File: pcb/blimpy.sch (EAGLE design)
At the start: 74 parts, among them J4 3-PIN SMD, J5 3-PIN SMD, J6 3-PIN SMD, J7 3-PIN SMD, Q1 mmbt2222, Q2 mmbt2222, Q3 DMG3415U, U1 RGB, U10 MAX17048, U2 AP2112-3.3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

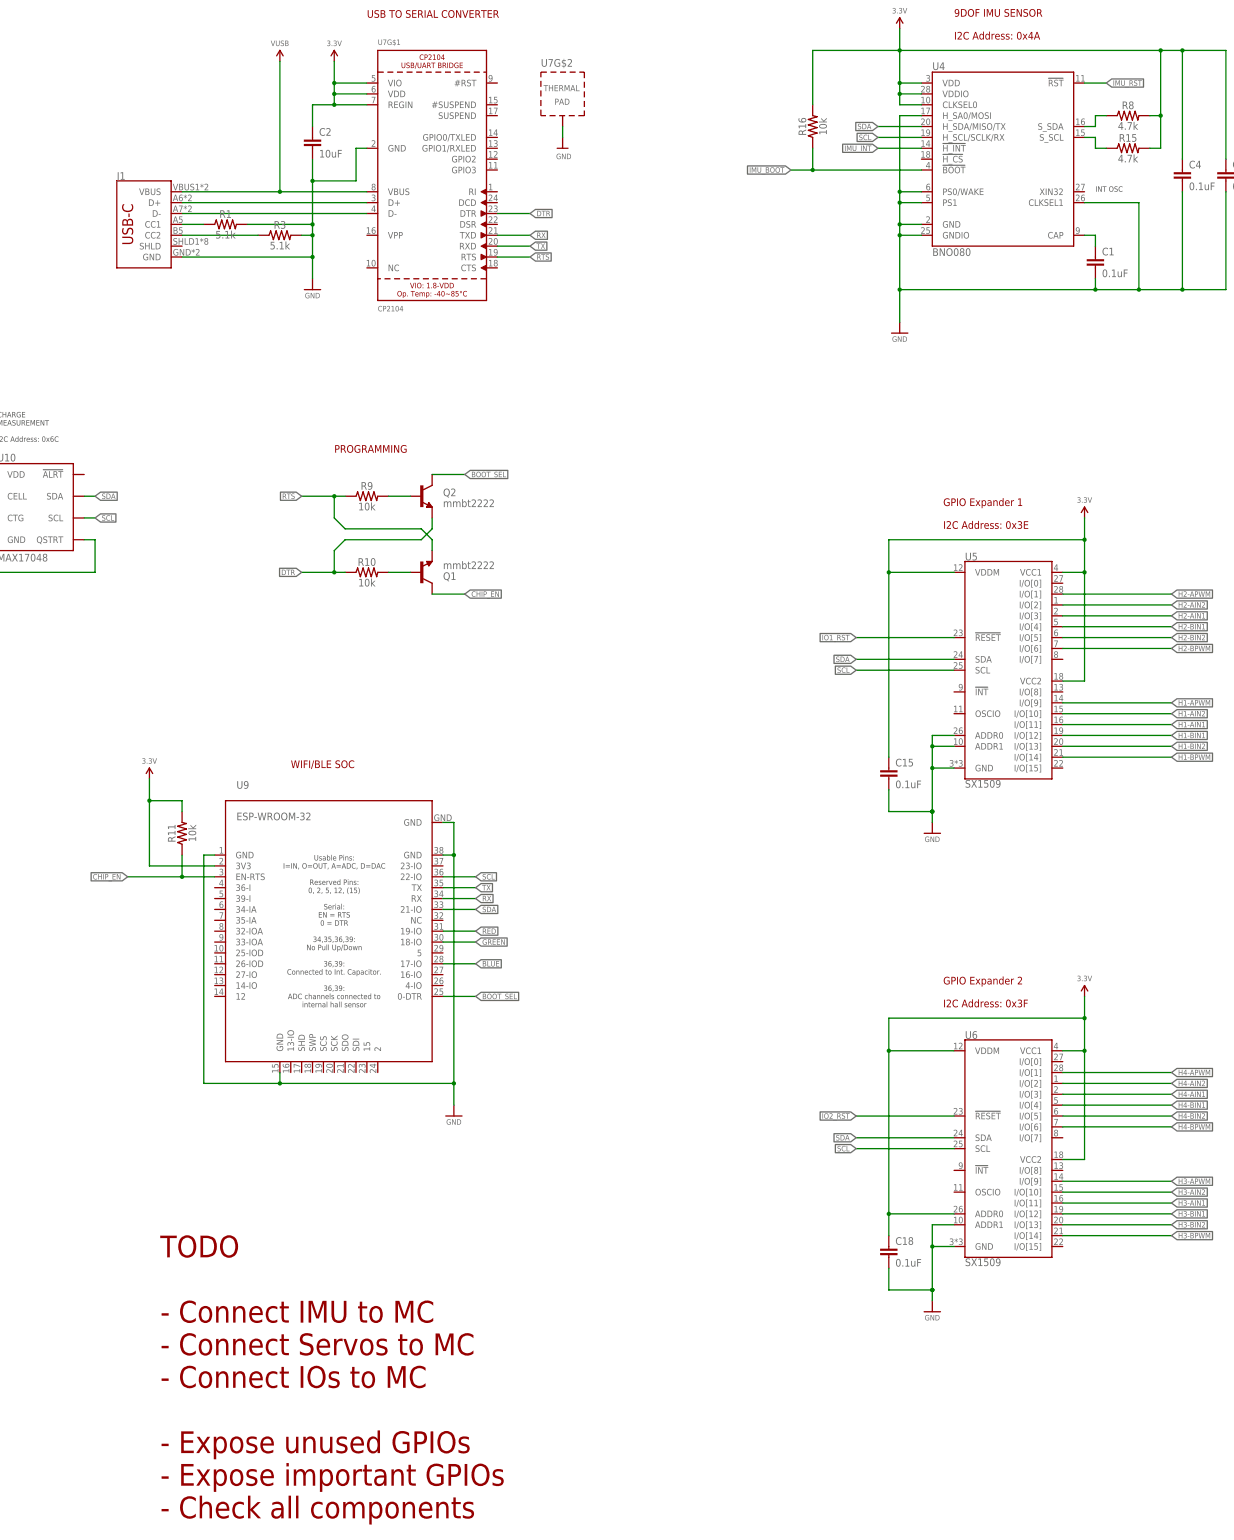
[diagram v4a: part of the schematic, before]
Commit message: connected all components
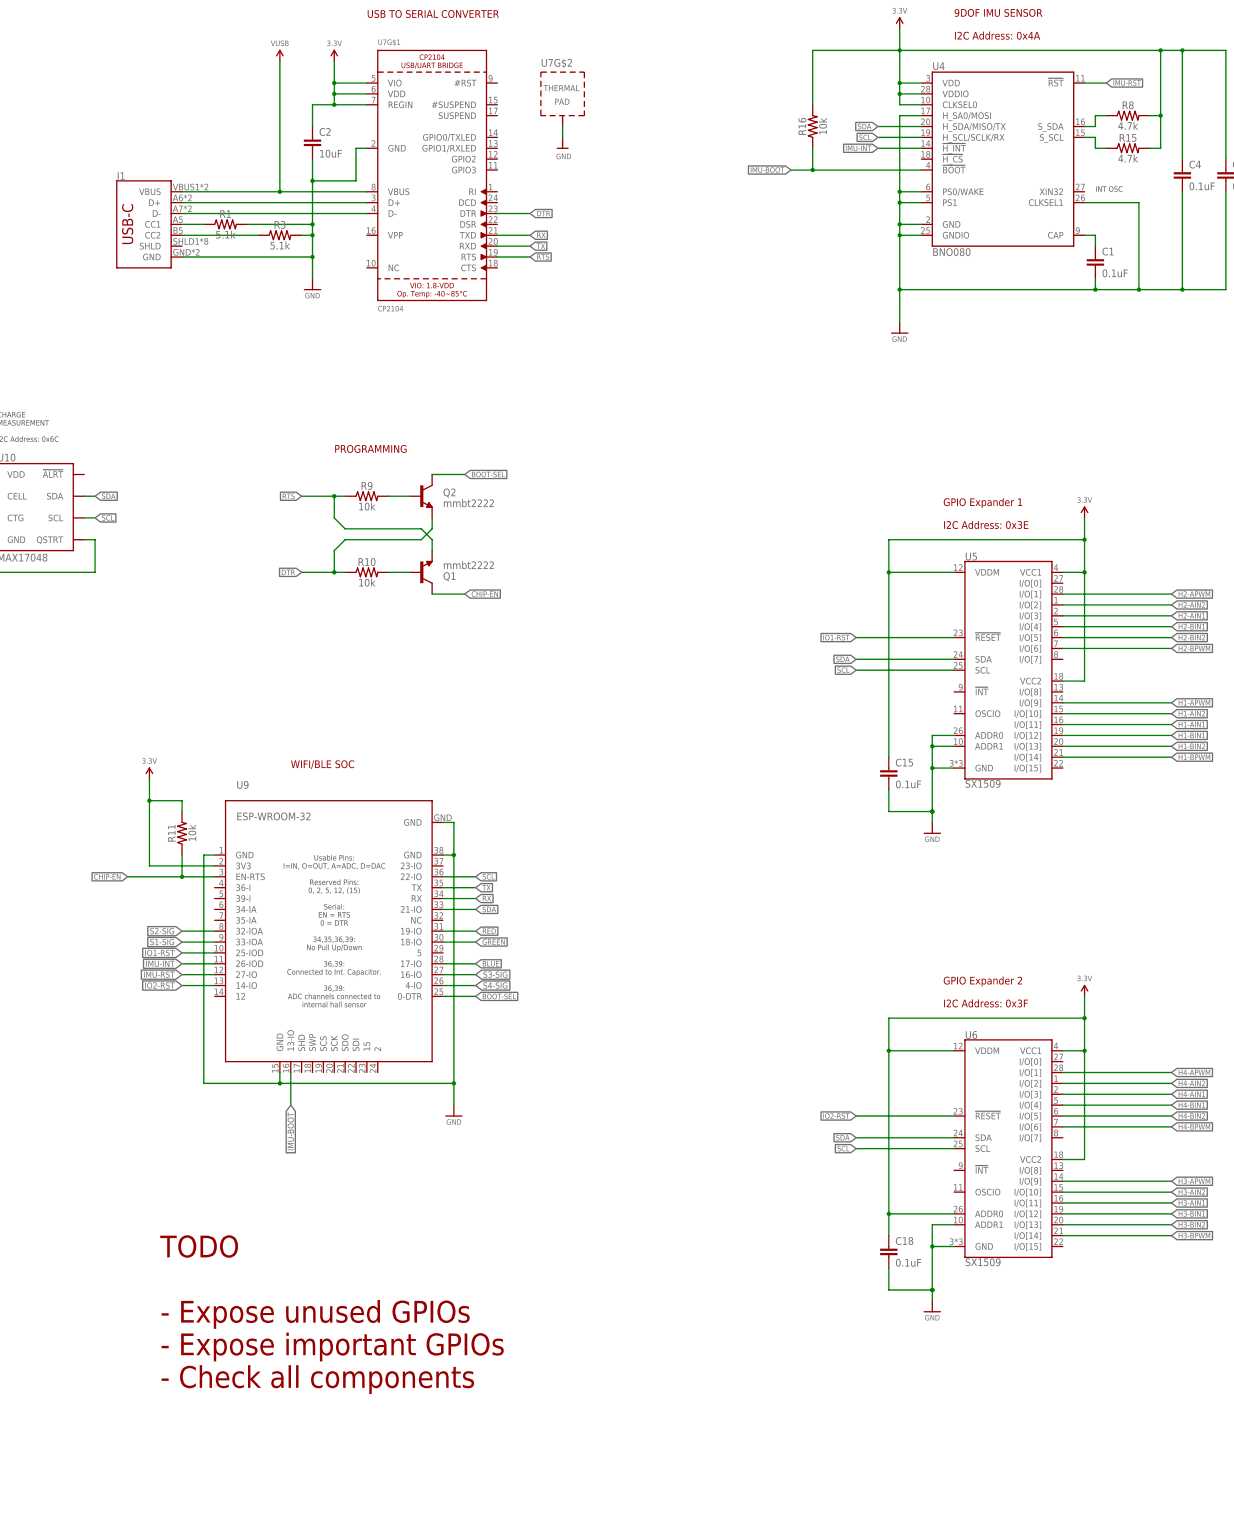
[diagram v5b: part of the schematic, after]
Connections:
- net BOOT_SEL renamed BOOT-SEL
- net CHIP_EN renamed CHIP-EN
- removed net IMU_BOOT: R16.1, U4.!BOOT
- removed net IMU_INT: U4.!H_INT
- removed net IMU_RST: U4.!RST
- removed net IO1_RST: U5.!RESET
- removed net IO2_RST: U6.!RESET
- new net IMU-BOOT: R16.1, U4.!BOOT, U9.13-IO
- new net IMU-INT: U4.!H_INT, U9.26-IOD
- new net IMU-RST: U4.!RST, U9.27-IO
- new net IO1-RST: U5.!RESET, U9.25-IOD
- new net IO2-RST: U6.!RESET, U9.14-IO
- net S1-SIG: now also U9.33-IOA
- net S2-SIG: now also U9.32-IOA
- net S3-SIG: now also U9.16-IO
- net S4-SIG: now also U9.4-IO
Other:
- note added: "TODO - Expose unused GPIOs - Expose important GPIOs - Check all components"
- note removed: "TODO - Connect IMU to MC - Connect Servos to MC - Connect IOs to MC - Expose unused GPIOs - Expose important GPIOs - Check all components"
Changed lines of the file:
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@@
 <text x="378.46" y="185.42" size="1.27" layer="97">INT OSC</text>
 <text x="160.02" y="-58.42" size="5.08" layer="94" align="top-left">TODO
-- Connect IMU to MC
-- Connect Servos to MC
-- Connect IOs to MC
 - Expose unused GPIOs
 - Expose important GPIOs
@@
 </segment>
 </net>
-<net name="BOOT_SEL" class="0">
-<segment>
-<wire x1="223.52" y1="119.38" x2="231.14" y2="119.38" width="0.1524" layer="91"/>
-<pinref part="Q2" gate="G$1" pin="C"/>
-<label x="231.14" y="119.38" size="1.27" layer="95" xref="yes"/>
-</segment>
-<segment>
-<pinref part="U9" gate="G$1" pin="0-DTR"/>
-<wire x1="226.06" y1="-2.54" x2="233.68" y2="-2.54" width="0.1524" layer="91"/>
-<label x="233.68" y="-2.54" size="1.27" layer="95" xref="yes"/>
-</segment>
-</net>
 <net name="N$2" class="0">
 <segment>
@@
 </segment>
 </net>
-<net name="CHIP_EN" class="0">
-<segment>
-<pinref part="U9" gate="G$1" pin="EN-RTS"/>
-<wire x1="172.72" y1="25.4" x2="165.1" y2="25.4" width="0.1524" layer="91"/>
-<label x="152.4" y="25.4" size="1.27" layer="95" rot="MR0" xref="yes"/>
-<wire x1="165.1" y1="25.4" x2="152.4" y2="25.4" width="0.1524" layer="91"/>
-<wire x1="165.1" y1="30.48" x2="165.1" y2="25.4" width="0.1524" layer="91"/>
-<junction x="165.1" y="25.4"/>
-<pinref part="R11" gate="G$1" pin="1"/>
-</segment>
-<segment>
-<wire x1="231.14" y1="91.44" x2="223.52" y2="91.44" width="0.1524" layer="91"/>
-<pinref part="Q1" gate="G$1" pin="C"/>
-<label x="231.14" y="91.44" size="1.27" layer="95" xref="yes"/>
-</segment>
-</net>
 <net name="RED" class="0">
 <segment>
@@
 </segment>
 </net>
-<net name="IMU_INT" class="0">
-<segment>
-<pinref part="U4" gate="U1" pin="!H_INT"/>
-<wire x1="337.82" y1="195.58" x2="327.66" y2="195.58" width="0.1524" layer="91"/>
-<label x="327.66" y="195.58" size="1.27" layer="95" rot="R180" xref="yes"/>
-</segment>
-</net>
-<net name="IMU_BOOT" class="0">
+<net name="IMU-BOOT" class="0">
 <segment>
 <pinref part="U4" gate="U1" pin="!BOOT"/>
@@
 <junction x="312.42" y="190.5"/>
 </segment>
-</net>
-<net name="IMU_RST" class="0">
-<segment>
-<pinref part="U4" gate="U1" pin="!RST"/>
-<wire x1="375.92" y1="210.82" x2="381" y2="210.82" width="0.1524" layer="91"/>
-<label x="381" y="210.82" size="1.27" layer="95" xref="yes"/>
+<segment>
+<pinref part="U9" gate="G$1" pin="13-IO"/>
+<wire x1="190.5" y1="-20.32" x2="190.5" y2="-27.94" width="0.1524" layer="91"/>
+<label x="190.5" y="-27.94" size="1.4224" layer="95" rot="R270" xref="yes"/>
 </segment>
 </net>
@@
 </segment>
 </net>
-<net name="IO2_RST" class="0">
+<net name="IO2-RST" class="0">
 <segment>
 <wire x1="322.58" y1="-30.48" x2="345.44" y2="-30.48" width="0.1524" layer="91"/>
@@
 <label x="322.58" y="-30.48" size="1.27" layer="95" rot="R180" xref="yes"/>
 </segment>
-</net>
-<net name="IO1_RST" class="0">
-<segment>
-<wire x1="322.58" y1="81.28" x2="345.44" y2="81.28" width="0.1524" layer="91"/>
-<pinref part="U5" gate="G$1" pin="!RESET"/>
-<label x="322.58" y="81.28" size="1.27" layer="95" rot="R180" xref="yes"/>
+<segment>
+<pinref part="U9" gate="G$1" pin="14-IO"/>
+<wire x1="172.72" y1="0" x2="165.1" y2="0" width="0.1524" layer="91"/>
+<label x="165.1" y="0" size="1.4224" layer="95" rot="R180" xref="yes"/>
 </segment>
 </net>
@@
 <label x="60.96" y="-66.04" size="1.4224" layer="95" xref="yes"/>
 </segment>
+<segment>
+<pinref part="U9" gate="G$1" pin="33-IOA"/>
+<wire x1="172.72" y1="10.16" x2="165.1" y2="10.16" width="0.1524" layer="91"/>
+<label x="165.1" y="10.16" size="1.4224" layer="95" rot="R180" xref="yes"/>
+</segment>
 </net>
 <net name="S2-SIG" class="0">
@@
 <label x="60.96" y="-81.28" size="1.4224" layer="95" xref="yes"/>
 </segment>
+<segment>
+<pinref part="U9" gate="G$1" pin="32-IOA"/>
+<wire x1="172.72" y1="12.7" x2="165.1" y2="12.7" width="0.1524" layer="91"/>
+<label x="165.1" y="12.7" size="1.4224" layer="95" rot="R180" xref="yes"/>
+</segment>
 </net>
 <net name="S3-SIG" class="0">
@@
 <label x="60.96" y="-96.52" size="1.4224" layer="95" xref="yes"/>
 </segment>
+<segment>
+<pinref part="U9" gate="G$1" pin="16-IO"/>
+<wire x1="226.06" y1="2.54" x2="233.68" y2="2.54" width="0.1524" layer="91"/>
+<label x="233.68" y="2.54" size="1.4224" layer="95" xref="yes"/>
+</segment>
 </net>
 <net name="S4-SIG" class="0">
@@
 <label x="60.96" y="-111.76" size="1.4224" layer="95" xref="yes"/>
 </segment>
-</net>
+<segment>
+<pinref part="U9" gate="G$1" pin="4-IO"/>
+<wire x1="226.06" y1="0" x2="233.68" y2="0" width="0.1524" layer="91"/>
+<label x="233.68" y="0" size="1.4224" layer="95" xref="yes"/>
+</segment>
+</net>
+<net name="IMU-INT" class="0">
+<segment>
+<pinref part="U9" gate="G$1" pin="26-IOD"/>
+<wire x1="172.72" y1="5.08" x2="165.1" y2="5.08" width="0.1524" layer="91"/>
+<label x="165.1" y="5.08" size="1.4224" layer="95" rot="R180" xref="yes"/>
+</segment>
+<segment>
+<pinref part="U4" gate="U1" pin="!H_INT"/>
+<wire x1="337.82" y1="195.58" x2="327.66" y2="195.58" width="0.1524" layer="91"/>
+<label x="327.66" y="195.58" size="1.27" layer="95" rot="R180" xref="yes"/>
+</segment>
+</net>
+<net name="IMU-RST" class="0">
+<segment>
+<pinref part="U9" gate="G$1" pin="27-IO"/>
+<wire x1="172.72" y1="2.54" x2="165.1" y2="2.54" width="0.1524" layer="91"/>
+<label x="165.1" y="2.54" size="1.4224" layer="95" rot="R180" xref="yes"/>
+</segment>
+<segment>
+<pinref part="U4" gate="U1" pin="!RST"/>
+<wire x1="375.92" y1="210.82" x2="381" y2="210.82" width="0.1524" layer="91"/>
+<label x="381" y="210.82" size="1.27" layer="95" xref="yes"/>
+</segment>
+</net>
+<net name="IO1-RST" class="0">
+<segment>
+<pinref part="U9" gate="G$1" pin="25-IOD"/>
+<wire x1="172.72" y1="7.62" x2="165.1" y2="7.62" width="0.1524" layer="91"/>
+<label x="165.1" y="7.62" size="1.4224" layer="95" rot="R180" xref="yes"/>
+</segment>
+<segment>
+<wire x1="322.58" y1="81.28" x2="345.44" y2="81.28" width="0.1524" layer="91"/>
+<pinref part="U5" gate="G$1" pin="!RESET"/>
+<label x="322.58" y="81.28" size="1.27" layer="95" rot="R180" xref="yes"/>
+</segment>
+</net>
+<net name="BOOT-SEL" class="0">
+<segment>
+<pinref part="U9" gate="G$1" pin="0-DTR"/>
+<wire x1="226.06" y1="-2.54" x2="233.68" y2="-2.54" width="0.1524" layer="91"/>
+<label x="233.68" y="-2.54" size="1.27" layer="95" xref="yes"/>
+</segment>
+<segment>
+<wire x1="223.52" y1="119.38" x2="231.14" y2="119.38" width="0.1524" layer="91"/>
+<pinref part="Q2" gate="G$1" pin="C"/>
+<label x="231.14" y="119.38" size="1.27" layer="95" xref="yes"/>
+</segment>
+</net>
+<net name="CHIP-EN" class="0">
+<segment>
+<wire x1="231.14" y1="91.44" x2="223.52" y2="91.44" width="0.1524" layer="91"/>
+<pinref part="Q1" gate="G$1" pin="C"/>
+<label x="231.14" y="91.44" size="1.27" layer="95" xref="yes"/>
+</segment>
+<segment>
+<pinref part="U9" gate="G$1" pin="EN-RTS"/>
+<wire x1="172.72" y1="25.4" x2="165.1" y2="25.4" width="0.1524" layer="91"/>
+<label x="152.4" y="25.4" size="1.27" layer="95" rot="MR0" xref="yes"/>
+<wire x1="165.1" y1="25.4" x2="152.4" y2="25.4" width="0.1524" layer="91"/>
+<wire x1="165.1" y1="30.48" x2="165.1" y2="25.4" width="0.1524" layer="91"/>
+<junction x="165.1" y="25.4"/>
+<pinref part="R11" gate="G$1" pin="1"/>
+</segment>
+</net>

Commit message: finished all traces
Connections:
- net IO2-RST: now also U9.4-IO; no longer U9.14-IO
- net S3-SIG: now also U9.23-IO; no longer U9.16-IO
- net S4-SIG: now also U9.16-IO; no longer U9.4-IO
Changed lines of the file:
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@@
 </segment>
 <segment>
-<pinref part="U9" gate="G$1" pin="14-IO"/>
-<wire x1="172.72" y1="0" x2="165.1" y2="0" width="0.1524" layer="91"/>
-<label x="165.1" y="0" size="1.4224" layer="95" rot="R180" xref="yes"/>
+<pinref part="U9" gate="G$1" pin="4-IO"/>
+<wire x1="226.06" y1="0" x2="233.68" y2="0" width="0.1524" layer="91"/>
+<label x="233.68" y="0" size="1.4224" layer="95" xref="yes"/>
 </segment>
 </net>
@@
 </segment>
 <segment>
+<pinref part="U9" gate="G$1" pin="23-IO"/>
+<wire x1="226.06" y1="27.94" x2="233.68" y2="27.94" width="0.1524" layer="91"/>
+<label x="233.68" y="27.94" size="1.4224" layer="95" xref="yes"/>
+</segment>
+</net>
+<net name="S4-SIG" class="0">
+<segment>
+<pinref part="J7" gate="J$1" pin="3"/>
+<wire x1="53.34" y1="-111.76" x2="60.96" y2="-111.76" width="0.1524" layer="91"/>
+<label x="60.96" y="-111.76" size="1.4224" layer="95" xref="yes"/>
+</segment>
+<segment>
 <pinref part="U9" gate="G$1" pin="16-IO"/>
 <wire x1="226.06" y1="2.54" x2="233.68" y2="2.54" width="0.1524" layer="91"/>
@@
 </segment>
 </net>
-<net name="S4-SIG" class="0">
-<segment>
-<pinref part="J7" gate="J$1" pin="3"/>
-<wire x1="53.34" y1="-111.76" x2="60.96" y2="-111.76" width="0.1524" layer="91"/>
-<label x="60.96" y="-111.76" size="1.4224" layer="95" xref="yes"/>
-</segment>
-<segment>
-<pinref part="U9" gate="G$1" pin="4-IO"/>
-<wire x1="226.06" y1="0" x2="233.68" y2="0" width="0.1524" layer="91"/>
-<label x="233.68" y="0" size="1.4224" layer="95" xref="yes"/>
-</segment>
-</net>
